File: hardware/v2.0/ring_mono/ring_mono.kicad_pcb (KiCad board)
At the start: 2 copper layers, 19.1 x 19 mm, 8 parts

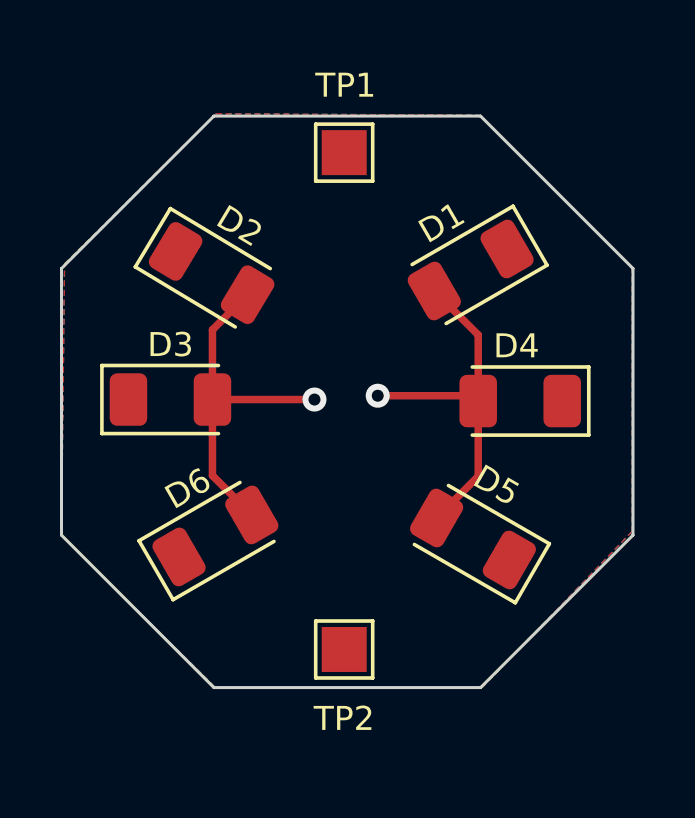
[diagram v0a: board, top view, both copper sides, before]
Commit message: Make mono PCB smaller
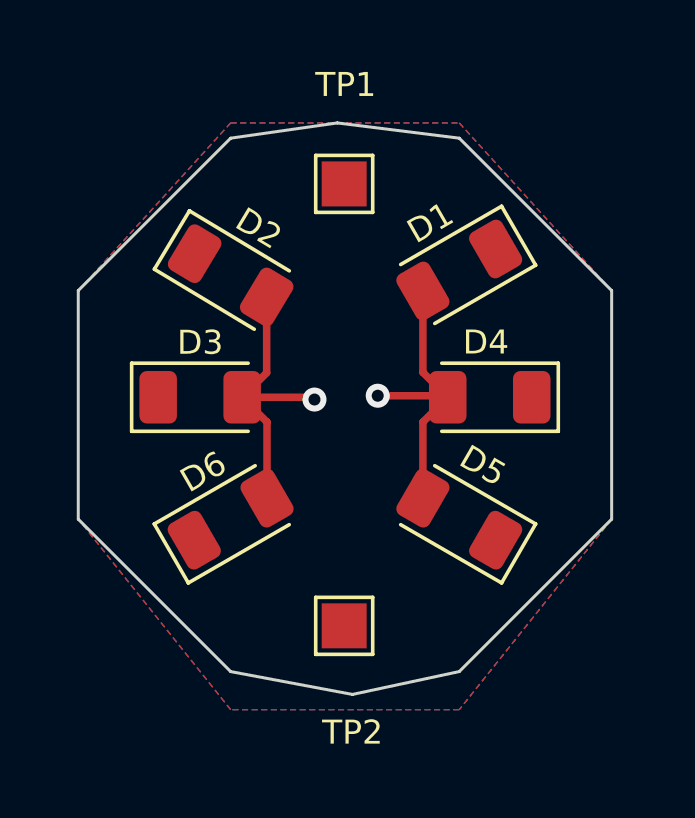
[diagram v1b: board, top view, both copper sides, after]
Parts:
- moved TP1 1.04 mm to (136.9, 75.7)
- moved D4 1.02 mm to (141.7, 82.8)
- moved D3 0.99 mm to (132.1, 82.8)
- moved D5 0.80 mm to (140.7, 86.9)
- moved TP2 0.79 mm to (136.9, 90.4)
- moved D6 0.76 mm to (133.1, 86.9)
- moved D2 0.64 mm to (133.1, 78.7)
- moved D1 0.38 mm to (140.7, 78.6)
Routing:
- net VCC: track 24.1 -> 19.8 mm
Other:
- board size 19.1 x 19 mm -> 17.8 x 19 mm
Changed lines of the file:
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@@
   (net 2 "/GND")
   (footprint "LED_SMD:LED_1206_3216Metric" (layer "F.Cu")
-    (at 141.1732 87.5284 150)
+    (at 140.716 86.868 150)
     (descr "LED SMD 1206 (3216 Metric), square (rectangular) end terminal, IPC_7351 nominal, (Body size source: http://www.tortai-tech.com/upload/download/2011102023233369053.pdf), generated with kicad-footprint-generator")
     (tags "LED")
@@
   )
   (footprint "LED_SMD:LED_1206_3216Metric" (layer "F.Cu")
-    (at 142.748 82.931 180)
+    (at 141.732 82.804 180)
     (descr "LED SMD 1206 (3216 Metric), square (rectangular) end terminal, IPC_7351 nominal, (Body size source: http://www.tortai-tech.com/upload/download/2011102023233369053.pdf), generated with kicad-footprint-generator")
     (tags "LED")
@@
   )
   (footprint "LED_SMD:LED_1206_3216Metric" (layer "F.Cu")
-    (at 141.097 78.5622 -150)
+    (at 140.716 78.5622 -150)
     (descr "LED SMD 1206 (3216 Metric), square (rectangular) end terminal, IPC_7351 nominal, (Body size source: http://www.tortai-tech.com/upload/download/2011102023233369053.pdf), generated with kicad-footprint-generator")
     (tags "LED")
@@
   )
   (footprint "TestPoint:TestPoint_Pad_1.5x1.5mm" (layer "F.Cu")
-    (at 136.8806 74.6506)
+    (at 136.8806 75.692)
     (descr "SMD rectangular pad as test Point, square 1.5mm side length")
     (tags "test point SMD pad rectangle square")
@@
     (property "ki_keywords" "test point tp")
     (attr exclude_from_pos_files)
-    (fp_text reference "TP1" (at 0.0508 -2.2352) (layer "F.SilkS")
+    (fp_text reference "TP1" (at 0.0508 -3.302) (layer "F.SilkS")
         (effects (font (size 0.8 0.8) (thickness 0.2)))
     )
@@
   )
   (footprint "TestPoint:TestPoint_Pad_1.5x1.5mm" (layer "F.Cu")
-    (at 136.8806 91.2114 180)
+    (at 136.8806 90.424 180)
     (descr "SMD rectangular pad as test Point, square 1.5mm side length")
     (tags "test point SMD pad rectangle square")
@@
     (property "ki_keywords" "test point tp")
     (attr exclude_from_pos_files)
-    (fp_text reference "TP2" (at 0 -2.3114) (layer "F.SilkS")
+    (fp_text reference "TP2" (at -0.2794 -3.556) (layer "F.SilkS")
         (effects (font (size 0.8 0.8) (thickness 0.2)))
     )
@@
   )
   (footprint "LED_SMD:LED_1206_3216Metric" (layer "F.Cu")
-    (at 132.588 87.4268 30)
+    (at 133.096 86.868 30)
     (descr "LED SMD 1206 (3216 Metric), square (rectangular) end terminal, IPC_7351 nominal, (Body size source: http://www.tortai-tech.com/upload/download/2011102023233369053.pdf), generated with kicad-footprint-generator")
     (tags "LED")
@@
   )
   (footprint "LED_SMD:LED_1206_3216Metric" (layer "F.Cu")
-    (at 132.461 78.6638 -31)
+    (at 133.096 78.74 -31)
     (descr "LED SMD 1206 (3216 Metric), square (rectangular) end terminal, IPC_7351 nominal, (Body size source: http://www.tortai-tech.com/upload/download/2011102023233369053.pdf), generated with kicad-footprint-generator")
     (tags "LED")
@@
   )
   (footprint "LED_SMD:LED_1206_3216Metric" (layer "F.Cu")
-    (at 131.0894 82.8802)
+    (at 132.08 82.804)
     (descr "LED SMD 1206 (3216 Metric), square (rectangular) end terminal, IPC_7351 nominal, (Body size source: http://www.tortai-tech.com/upload/download/2011102023233369053.pdf), generated with kicad-footprint-generator")
     (tags "LED")
@@
     )
   )
-  (gr_circle (center 136.906 82.6516) (end 139.954 82.7786)
-    (stroke (width 0.15) (type solid)) (fill solid) (layer "B.Mask"))
-  (gr_poly
-    (pts
-      (xy 146.5072 78.5114)
-      (xy 146.5072 87.4014)
-      (xy 141.4272 92.4814)
-      (xy 132.5372 92.4814)
-      (xy 127.4572 87.4014)
-      (xy 127.4572 78.5114)
-      (xy 132.5372 73.4314)
-      (xy 141.4272 73.4314)
-    )
-    (stroke (width 0.1) (type solid)) (fill none) (layer "Edge.Cuts"))
-  (segment (start 141.348 82.931) (end 141.1702 82.7532) (width 0.25) (layer "F.Cu") (net 1))
-  (segment (start 141.348 85.441164) (end 139.960764 86.8284) (width 0.25) (layer "F.Cu") (net 1))
-  (segment (start 141.348 82.931) (end 141.348 80.725636) (width 0.25) (layer "F.Cu") (net 1))
-  (segment (start 132.4894 80.556487) (end 132.4894 82.8802) (width 0.25) (layer "F.Cu") (net 1))
-  (segment (start 141.1702 82.7532) (end 137.9982 82.7532) (width 0.25) (layer "F.Cu") (net 1))
-  (segment (start 132.4894 82.8802) (end 132.4894 85.415764) (width 0.25) (layer "F.Cu") (net 1))
-  (segment (start 141.348 80.725636) (end 139.884564 79.2622) (width 0.25) (layer "F.Cu") (net 1))
-  (segment (start 138.0998 82.8548) (end 137.9982 82.7532) (width 0.25) (layer "F.Cu") (net 1))
-  (segment (start 132.4894 85.415764) (end 133.800436 86.7268) (width 0.25) (layer "F.Cu") (net 1))
-  (segment (start 141.348 82.931) (end 141.348 85.441164) (width 0.25) (layer "F.Cu") (net 1))
-  (segment (start 133.661034 79.384853) (end 132.4894 80.556487) (width 0.25) (layer "F.Cu") (net 1))
-  (segment (start 132.4894 82.8802) (end 135.89 82.8802) (width 0.25) (layer "F.Cu") (net 1))
+  (gr_line (start 145.796 86.868) (end 140.716 91.948)
+    (stroke (width 0.1) (type solid)) (layer "Edge.Cuts"))
+  (gr_line (start 140.716 74.168) (end 145.796 79.248)
+    (stroke (width 0.1) (type solid)) (layer "Edge.Cuts"))
+  (gr_line (start 128.016 79.248) (end 128.016 86.868)
+    (stroke (width 0.1) (type solid)) (layer "Edge.Cuts"))
+  (gr_line (start 133.096 91.948) (end 137.16 92.71)
+    (stroke (width 0.1) (type solid)) (layer "Edge.Cuts"))
+  (gr_line (start 137.16 92.71) (end 140.716 91.948)
+    (stroke (width 0.1) (type solid)) (layer "Edge.Cuts"))
+  (gr_line (start 145.796 79.248) (end 145.796 86.868)
+    (stroke (width 0.1) (type solid)) (layer "Edge.Cuts"))
+  (gr_line (start 140.716 74.168) (end 136.652 73.66)
+    (stroke (width 0.1) (type solid)) (layer "Edge.Cuts"))
+  (gr_line (start 136.652 73.66) (end 133.096 74.168)
+    (stroke (width 0.1) (type solid)) (layer "Edge.Cuts"))
+  (gr_line (start 128.016 86.868) (end 133.096 91.948)
+    (stroke (width 0.1) (type solid)) (layer "Edge.Cuts"))
+  (gr_line (start 128.016 79.248) (end 133.096 74.168)
+    (stroke (width 0.1) (type solid)) (layer "Edge.Cuts"))
+  (segment (start 139.503564 83.632436) (end 140.332 82.804) (width 0.25) (layer "F.Cu") (net 1))
+  (segment (start 139.503564 81.975564) (end 139.503564 79.2622) (width 0.25) (layer "F.Cu") (net 1))
+  (segment (start 140.332 82.804) (end 139.503564 81.975564) (width 0.25) (layer "F.Cu") (net 1))
+  (segment (start 133.48 82.804) (end 134.308436 83.632436) (width 0.25) (layer "F.Cu") (net 1))
+  (segment (start 133.48 82.804) (end 135.8138 82.804) (width 0.25) (layer "F.Cu") (net 1))
+  (segment (start 135.8138 82.804) (end 135.89 82.8802) (width 0.25) (layer "F.Cu") (net 1))
+  (segment (start 134.308436 83.632436) (end 134.308436 86.168) (width 0.25) (layer "F.Cu") (net 1))
+  (segment (start 134.296034 81.987966) (end 134.296034 79.461053) (width 0.25) (layer "F.Cu") (net 1))
+  (segment (start 140.2812 82.7532) (end 140.332 82.804) (width 0.25) (layer "F.Cu") (net 1))
+  (segment (start 133.48 82.804) (end 134.296034 81.987966) (width 0.25) (layer "F.Cu") (net 1))
+  (segment (start 139.503564 86.168) (end 139.503564 83.632436) (width 0.25) (layer "F.Cu") (net 1))
+  (segment (start 137.9982 82.7532) (end 140.2812 82.7532) (width 0.25) (layer "F.Cu") (net 1))
   (via (at 135.89 82.8802) (size 0.8) (drill 0.4) (layers "F.Cu" "B.Cu") (net 1))
   (via (at 137.9982 82.7532) (size 0.8) (drill 0.4) (layers "F.Cu" "B.Cu") (net 1))
@@
     (polygon
       (pts
-        (xy 132.6134 73.3552)
-        (xy 141.4018 73.406)
-        (xy 146.4818 78.4606)
-        (xy 146.4818 87.2744)
-        (xy 141.478 92.4814)
-        (xy 132.5626 92.456)
-        (xy 127.4572 87.4268)
-        (xy 127.5588 78.359)
+        (xy 133.096 73.66)
+        (xy 140.716 73.66)
+        (xy 145.796 79.248)
+        (xy 145.796 86.868)
+        (xy 140.716 93.218)
+        (xy 133.096 93.218)
+        (xy 128.016 86.868)
+        (xy 128.016 79.248)
       )
     )
@@
     (polygon
       (pts
-        (xy 132.6134 73.35239)
-        (xy 141.4018 73.40319)
-        (xy 146.4818 78.45779)
-        (xy 146.4818 87.27159)
-        (xy 141.478 92.47859)
-        (xy 132.5626 92.45319)
-        (xy 127.4572 87.42399)
-        (xy 127.5588 78.35619)
+        (xy 133.096 73.66)
+        (xy 140.716 73.66)
+        (xy 145.796 79.248)
+        (xy 145.796 86.868)
+        (xy 140.716 93.218)
+        (xy 133.096 93.218)
+        (xy 128.016 86.868)
+        (xy 128.016 79.248)
       )
     )
@@
     (polygon
       (pts
-        (xy 132.5626 92.5576)
+        (xy 133.096 93.218)
         (xy 132.588 89.7128)
         (xy 141.478 89.8398)
-        (xy 141.478 92.4814)
+        (xy 140.716 93.218)
       )
     )
@@
       (pts
         (xy 132.6642 76.073)
-        (xy 132.6896 73.406)
-        (xy 141.4526 73.4314)
+        (xy 133.096 73.66)
+        (xy 140.716 73.66)
         (xy 141.4526 76.1238)
       )
